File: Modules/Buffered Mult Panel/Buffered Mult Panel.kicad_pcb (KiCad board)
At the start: 2 copper layers, 48 x 175 mm, 44 parts, among them J1 TS_Jack_6.35mm_Sw, J10 TS_Jack_6.35mm_Sw, J100 IDC_02x05, J11 TS_Jack_6.35mm_Sw, J12 TS_Jack_6.35mm_Sw, J13 TS_Jack_6.35mm_Sw, J14 TS_Jack_6.35mm_Sw, J15 TS_Jack_6.35mm_Sw, J16 TS_Jack_6.35mm_Sw, J2 TS_Jack_6.35mm_Sw, J3 TS_Jack_6.35mm_Sw, J4 TS_Jack_6.35mm_Sw, J5 TS_Jack_6.35mm_Sw, J6 TS_Jack_6.35mm_Sw, J7 TS_Jack_6.35mm_Sw, J8 TS_Jack_6.35mm_Sw, J9 TS_Jack_6.35mm_Sw, U1 TL074, U2 TL074, U3 TL074

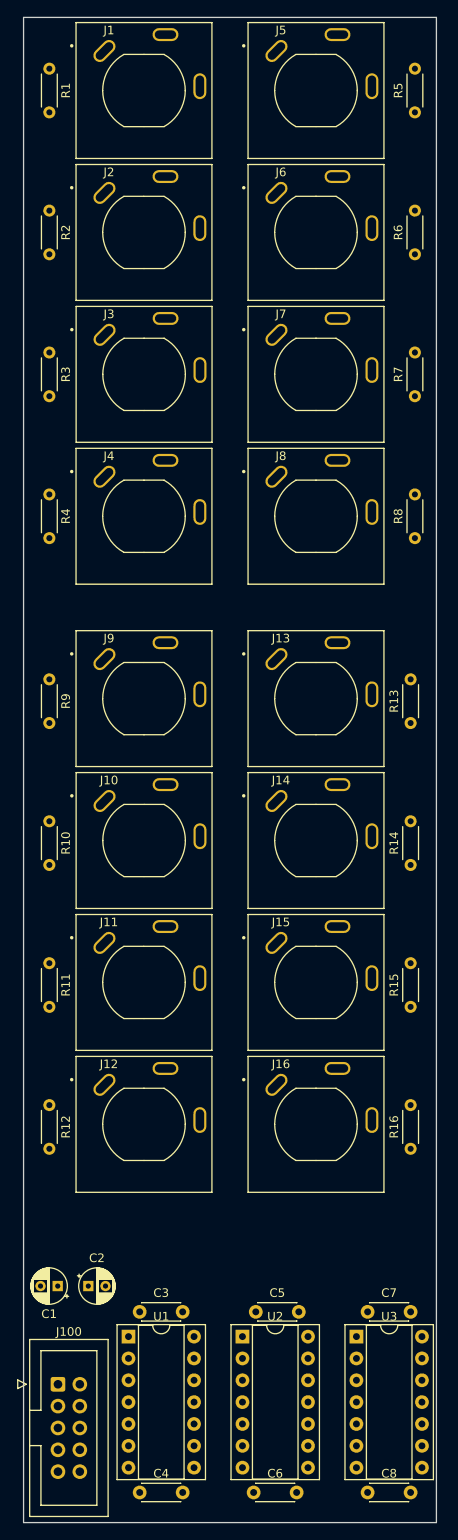
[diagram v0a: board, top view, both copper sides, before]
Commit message: Started moving components to the back
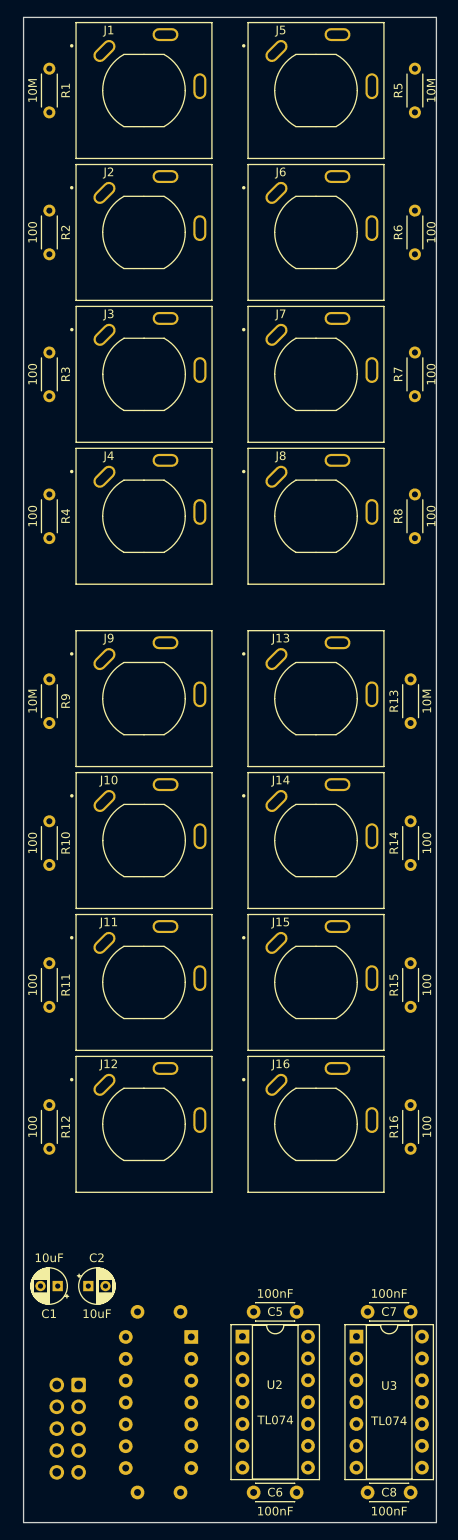
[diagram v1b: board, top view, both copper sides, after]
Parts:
- C3, C4, J100, U1: moved to B.Cu
- moved U1 7.30 mm to (45.5, 190.9), turned to 180 degrees
- moved C3 4.75 mm to (44.2, 188.0), turned to 180 degrees
- moved C4 4.75 mm to (44.2, 209.0), turned to 180 degrees
- moved J100 2.40 mm to (32.4, 196.5), turned to 180 degrees
- moved C5 0.25 mm to (52.8, 188.0)

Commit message: Finished flipping devices
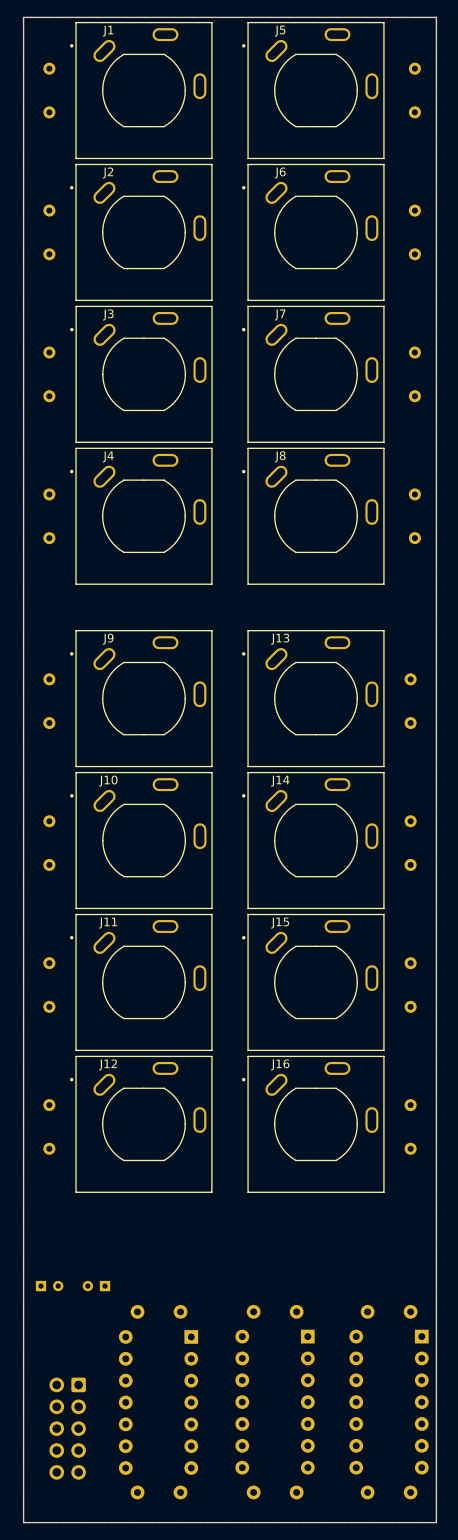
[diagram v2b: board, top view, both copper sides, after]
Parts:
- C1, C2, C5, C6, C7, C8, R1, R10, R11, R12, R13, R14, R15, R16, R2, R3, R4, R5, R6, R7, R8, R9, U2, U3: moved to B.Cu
- moved U2 7.60 mm to (59.0, 190.9), turned to 180 degrees
- moved U3 7.60 mm to (72.3, 190.9), turned to 180 degrees
- moved C5 5.00 mm to (57.8, 188.0), turned to 180 degrees
- moved C6 5.00 mm to (57.8, 209.0), turned to 180 degrees
- moved C7 5.00 mm to (71.0, 188.0), turned to 180 degrees
- moved C8 5.00 mm to (71.0, 209.0), turned to 180 degrees
- moved C2 1.95 mm to (35.5, 185.0), turned to 180 degrees
- moved C1 1.95 mm to (28.0, 185.0), turned to 0 degrees
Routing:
- added copper zone on F.Cu, net GND

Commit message: Routed traces
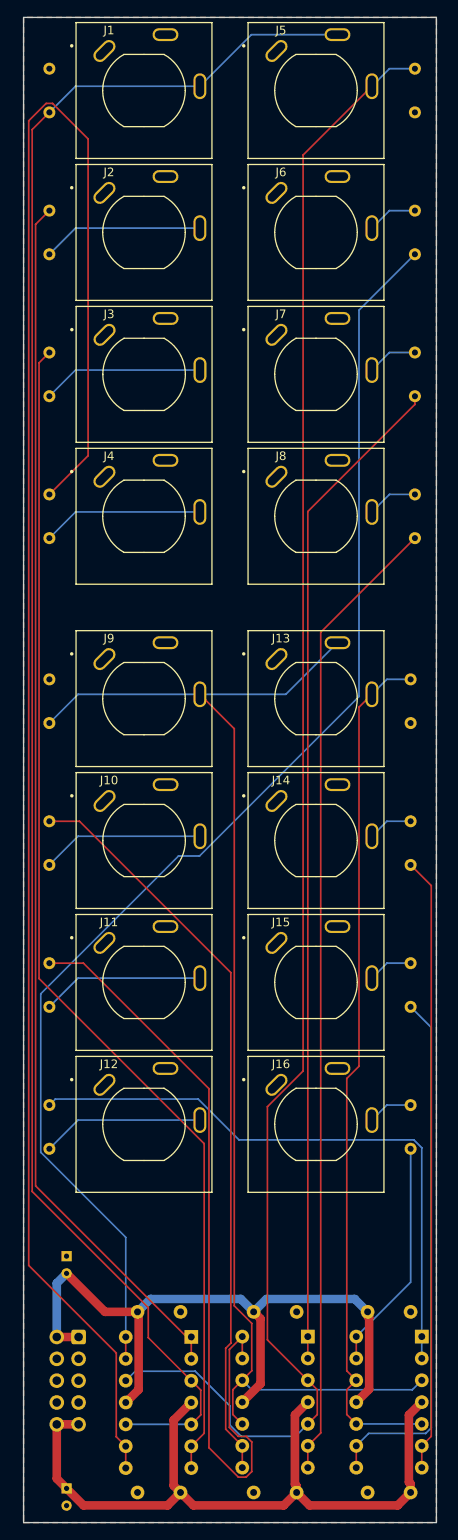
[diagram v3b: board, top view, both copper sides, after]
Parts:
- moved C1 23.7 mm to (31.0, 208.5), turned to -90 degrees
- moved C3 21.0 mm to (44.2, 209.0)
- moved C4 21.0 mm to (44.2, 188.0)
- moved C5 21.0 mm to (57.8, 209.0)
- moved C6 21.0 mm to (57.8, 188.0)
- moved C7 21.0 mm to (71.0, 209.0)
- moved C8 21.0 mm to (71.0, 188.0)
- moved C2 5.66 mm to (31.0, 181.5), turned to -90 degrees
- moved J100 5.58 mm to (32.4, 190.9)
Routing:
- net Net-(U1C--): track 0.00 -> 214.0 mm
- net Net-(U1A-+): track 0.00 -> 206.8 mm
- net Net-(U1D-+): track 0.00 -> 195.9 mm
- net Net-(U1D--): track 0.00 -> 152.0 mm
- net Net-(U2C-+): track 0.00 -> 147.8 mm
- net Net-(U1A--): track 0.00 -> 142.0 mm
- net Net-(U1B--): track 0.00 -> 138.8 mm
- net Net-(U2A--): track 0.00 -> 117.0 mm
- net Net-(U2B--): track 0.00 -> 113.2 mm
- net Net-(U3B-+): track 0.00 -> 100.3 mm
- net Net-(U2D--): track 0.00 -> 93.5 mm
- net +12V: track 0.00 -> 88.4 mm
- net Net-(U2C--): track 0.00 -> 87.0 mm
- net -12V: track 0.00 -> 83.9 mm
- net Net-(U3B--): track 0.00 -> 71.5 mm
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- added copper zone on B.Cu, net GND

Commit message: Adjusted routing
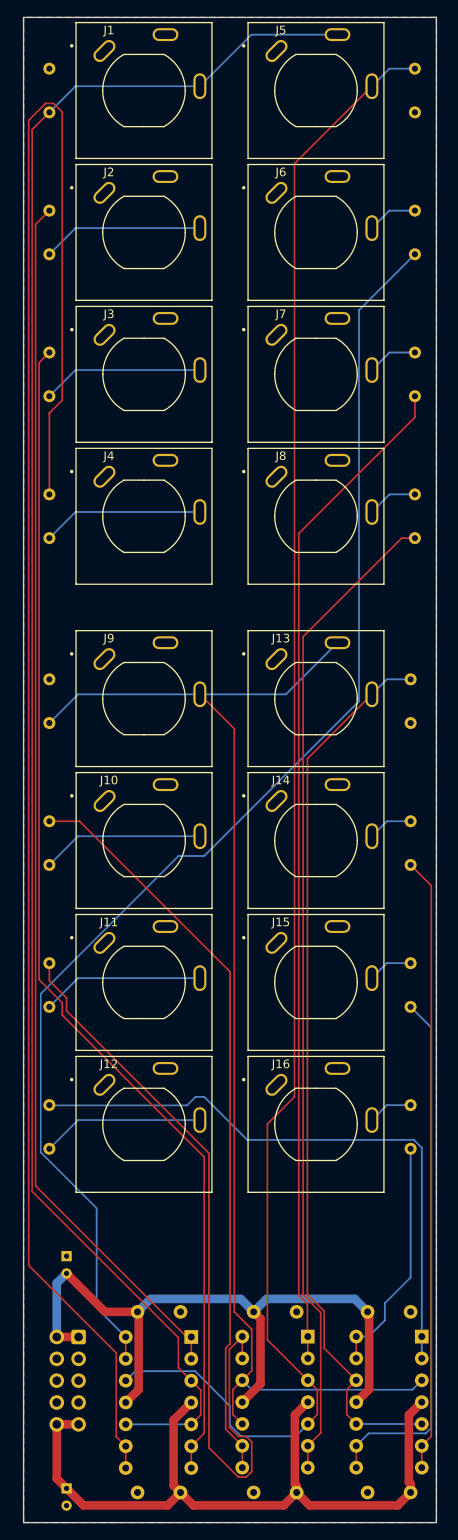
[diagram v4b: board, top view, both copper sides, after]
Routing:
- net Net-(U3B-+): track 100.3 -> 104.0 mm
- net Net-(U2B--): track 113.2 -> 115.8 mm
- net Net-(U1C--): track 214.0 -> 211.6 mm
- net Net-(U2D--): track 93.5 -> 91.1 mm
- net Net-(U2A--): track 117.0 -> 117.9 mm
- net Net-(U3D--): track 27.0 -> 27.8 mm

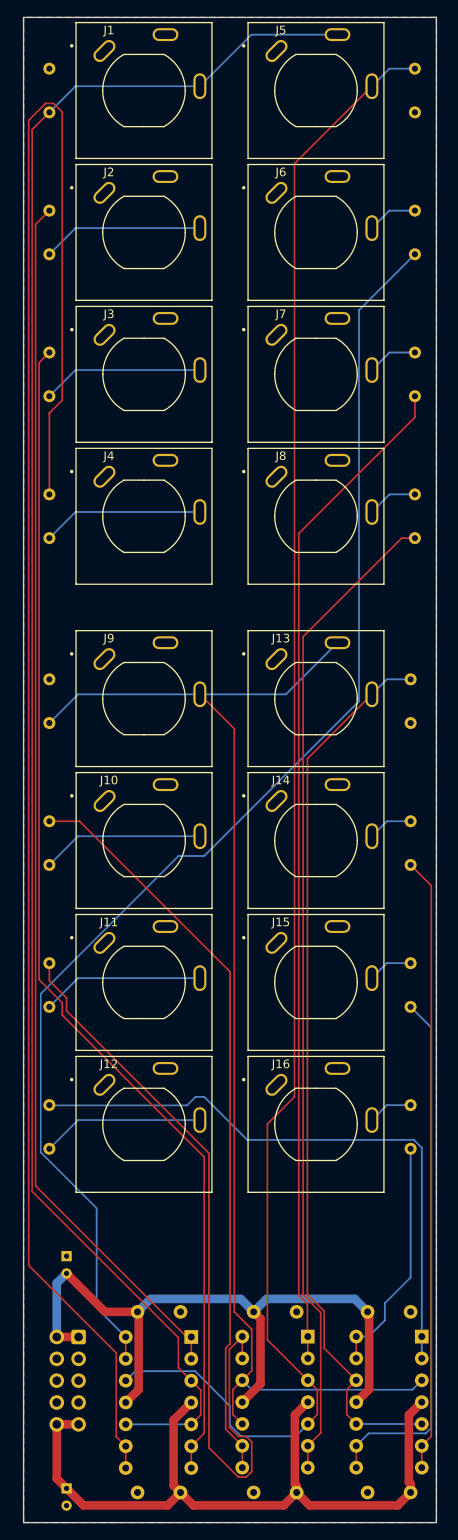
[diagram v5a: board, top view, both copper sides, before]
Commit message: Repositioned components on PCB
... in order to match front panel
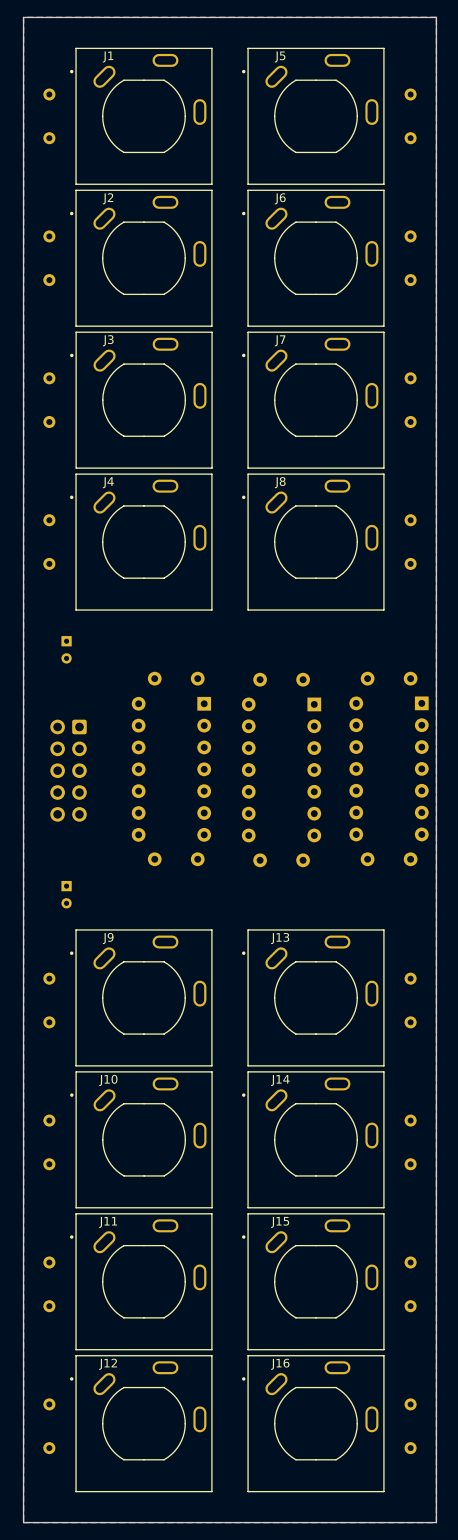
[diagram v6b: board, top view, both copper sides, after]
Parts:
- moved C3 73.6 mm to (46.2, 135.4)
- moved C4 73.6 mm to (46.2, 114.4)
- moved U1 73.6 mm to (47.0, 117.3)
- moved C7 73.6 mm to (71.0, 135.4)
- moved C8 73.6 mm to (71.0, 114.4)
- moved U3 73.6 mm to (72.3, 117.3)
- moved C5 73.5 mm to (58.5, 135.5)
- moved C6 73.5 mm to (58.5, 114.5)
- moved U2 73.5 mm to (59.8, 117.4)
- moved C2 71.5 mm to (31.0, 110.0)
- moved J100 70.9 mm to (32.5, 120.0)
- moved C1 70.0 mm to (31.0, 138.5)
- moved J10 34.8 mm to (40.0, 168.0)
- moved J11 34.8 mm to (40.0, 184.5)
- moved J12 34.8 mm to (40.0, 201.0)
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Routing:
- net Net-(U1C--): track 211.6 -> 0.00 mm
- net Net-(U1A-+): track 206.8 -> 0.00 mm
- net Net-(U1D-+): track 195.9 -> 0.00 mm
- net Net-(U1D--): track 152.3 -> 0.00 mm
- net Net-(U2C-+): track 147.8 -> 0.00 mm
- net Net-(U1A--): track 142.0 -> 0.00 mm
- net Net-(U1B--): track 138.8 -> 0.00 mm
- net Net-(U2A--): track 117.9 -> 0.00 mm
- net Net-(U2B--): track 115.8 -> 0.00 mm
- net Net-(U3B-+): track 104.0 -> 0.00 mm
- net Net-(U2D--): track 91.1 -> 0.00 mm
- net +12V: track 88.4 -> 0.00 mm
- net Net-(U2C--): track 86.9 -> 0.00 mm
- net -12V: track 83.9 -> 0.00 mm
- net Net-(U3B--): track 71.5 -> 0.00 mm
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
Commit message: Re-routed PCB
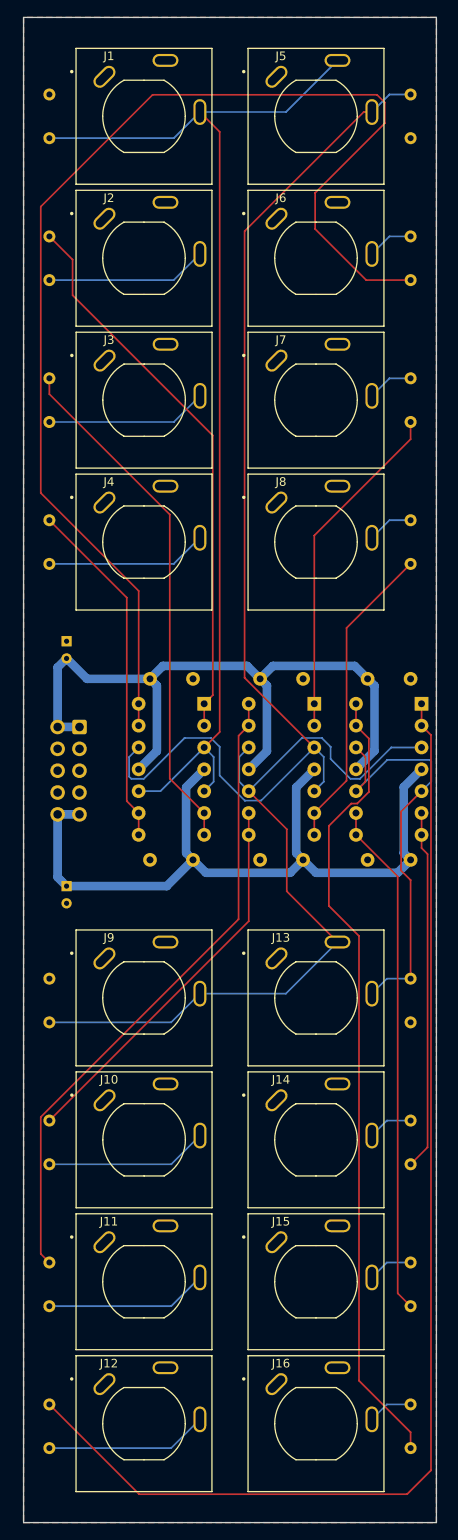
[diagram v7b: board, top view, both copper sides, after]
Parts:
- moved C3 0.55 mm to (45.7, 135.4)
- moved C4 0.55 mm to (45.7, 114.4)
- moved C6 0.10 mm to (58.5, 114.4)
- moved U2 0.08 mm to (59.8, 117.3)
- moved C7 0.07 mm to (71.0, 135.4)
- moved U3 0.05 mm to (72.3, 117.3)
- moved C5 0.05 mm to (58.5, 135.4)
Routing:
- net Net-(U1D--): track 0.00 -> 142.4 mm
- net Net-(U3A--): track 0.00 -> 139.4 mm
- net Net-(U1D-+): track 0.00 -> 130.2 mm
- net Net-(U1A-+): track 0.00 -> 128.5 mm
- net Net-(U3D--): track 0.00 -> 93.4 mm
- net Net-(U2C-+): track 0.00 -> 92.1 mm
- net +12V: track 0.00 -> 90.2 mm
- net -12V: track 0.00 -> 84.6 mm
- net Net-(U2D--): track 0.00 -> 75.4 mm
- net Net-(U1A--): track 0.00 -> 65.2 mm
- net Net-(U1B--): track 0.00 -> 60.5 mm
- net Net-(U3C--): track 0.00 -> 60.0 mm
- net Net-(U3B-+): track 0.00 -> 48.7 mm
- net Net-(U2C--): track 0.00 -> 45.4 mm
- net Net-(U3B--): track 0.00 -> 41.9 mm
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
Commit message: Removed normalling of input jacks directly to GND
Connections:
- J1 pad TN: GND -> unconnected-(J1-PadTN)
- J9 pad TN: GND -> unconnected-(J9-PadTN)
